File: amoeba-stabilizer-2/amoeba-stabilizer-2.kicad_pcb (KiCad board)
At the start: 2 copper layers, 31.8 x 20.8 mm, 24 parts

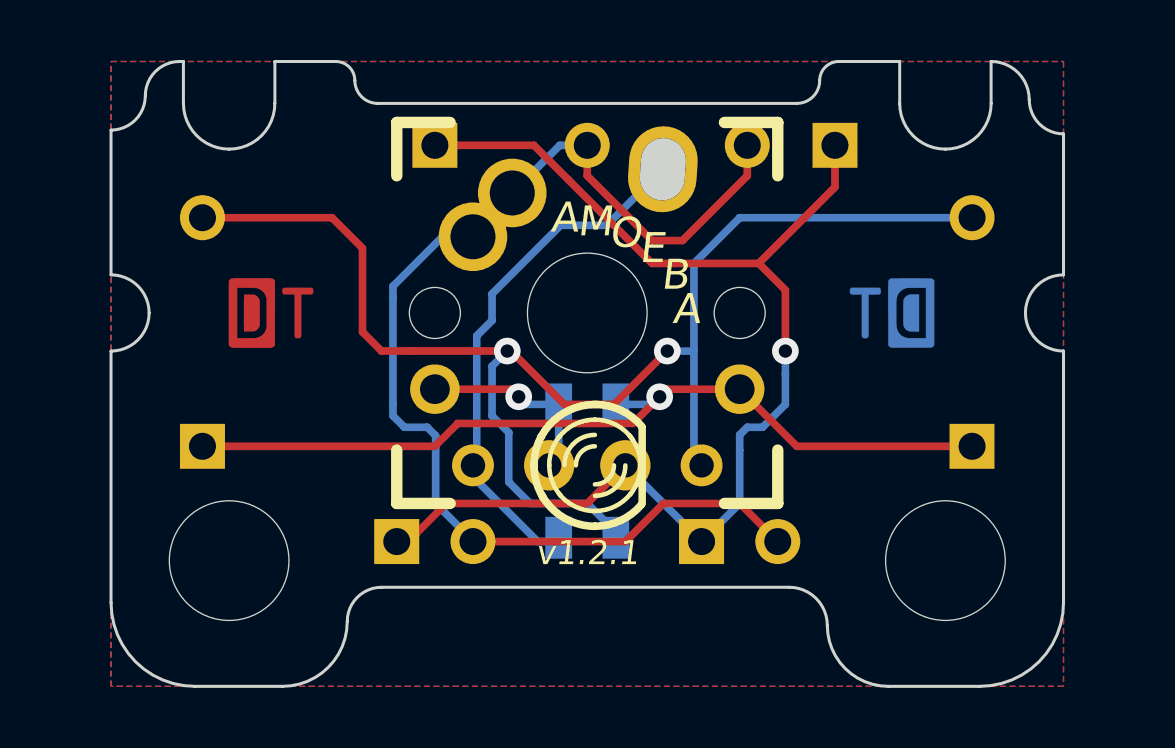
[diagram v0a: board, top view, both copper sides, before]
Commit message: Widened 2u pcb.
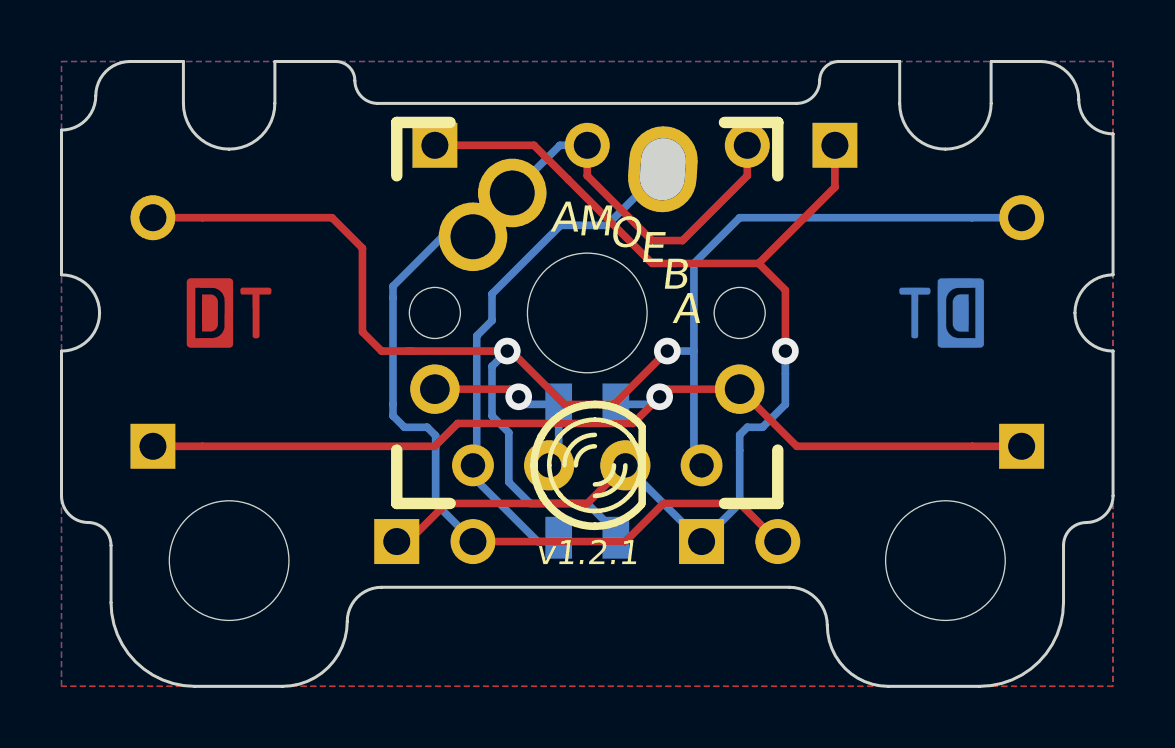
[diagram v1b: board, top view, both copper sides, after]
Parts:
- moved G*** 1.65 mm to (260.7, 110.5)
- moved G*** 1.40 mm to (237.0, 110.5)
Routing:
- net /key/SR0: track 47.3 -> 50.6 mm
- net /key/LR0: track 28.8 -> 32.1 mm
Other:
- board size 31.8 x 20.8 mm -> 35.1 x 20.8 mm

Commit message: Updates to amoeba 1u and 2u.
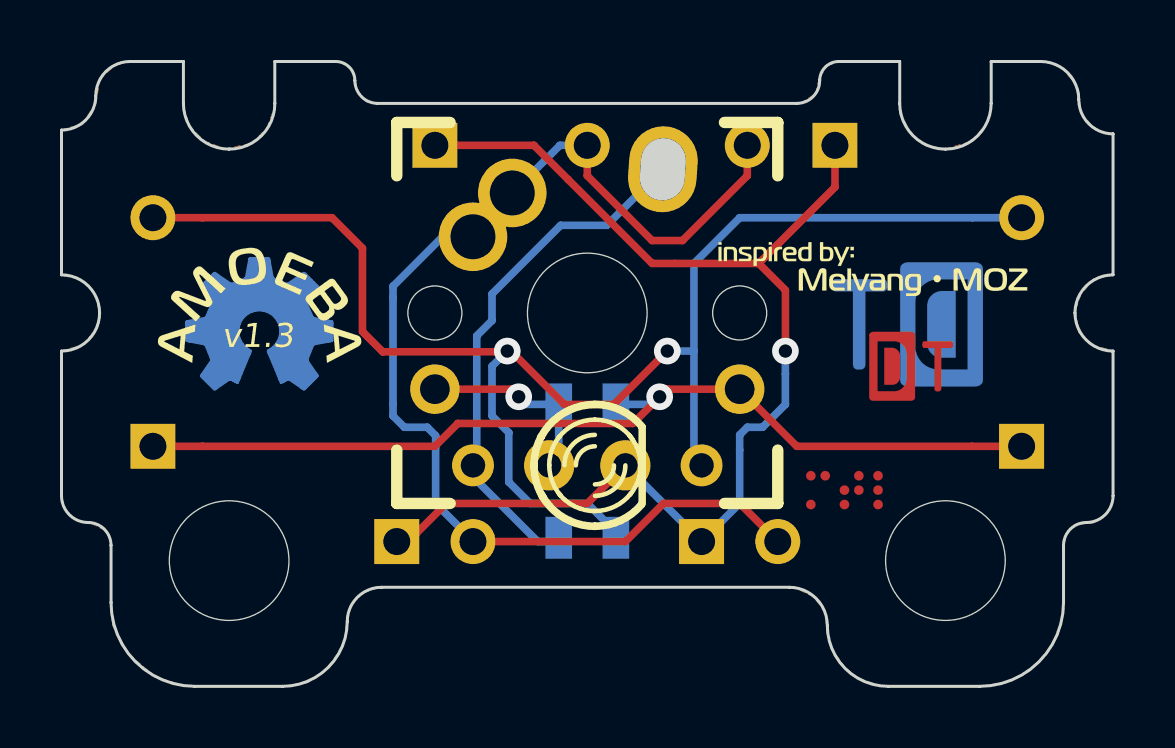
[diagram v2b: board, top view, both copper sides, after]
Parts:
- removed G***: DT-Logo, DT-Logo
- removed G***: DT-Logo-Rev, DT-Logo-Rev
- added amoeba-round: G***, amoeba-round, F.Cu at (238.0, 110.2)
- added amoeba-round-rev: G***, amoeba-round-rev, F.Cu at (248.9, 109.1)
- added dt-logo: G***, dt-logo, F.Cu at (259.7, 112.3)
- added dt-logo-big-rev: G***, dt-logo-big-rev, F.Cu at (259.6, 110.9)
- added labels-melvang-moz: G***, labels-melvang-moz, F.Cu at (258.4, 109.0)
- added mtl-braille: G***, mtl-braille, F.Cu at (257.5, 116.4)
- added osh-logo-rev: G***, osh-logo-rev, F.Cu at (238.0, 110.9)
- S0: footprint ALPS_CHERRY_PCB_100H -> ALPS_CHERRY_ZEAL_PCB_100H
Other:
- board text added: "v1.3"
- board text removed: "A"
- board text removed: "B"
- board text removed: "E"
- board text removed: "M"
- board text removed: "O"
- board text removed: "v1.2.1"
